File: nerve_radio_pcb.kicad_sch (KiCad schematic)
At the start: 25 parts, among them J1 BF030-20A-B1-0360-0277-0600-LB, J2 5V GPIO Breakout, J3 3V SPI Breakout, J4 Battery, U1 TXB0104QPWRQ1, U2 TPSM82903, U3 XBP9B-DMWT-002

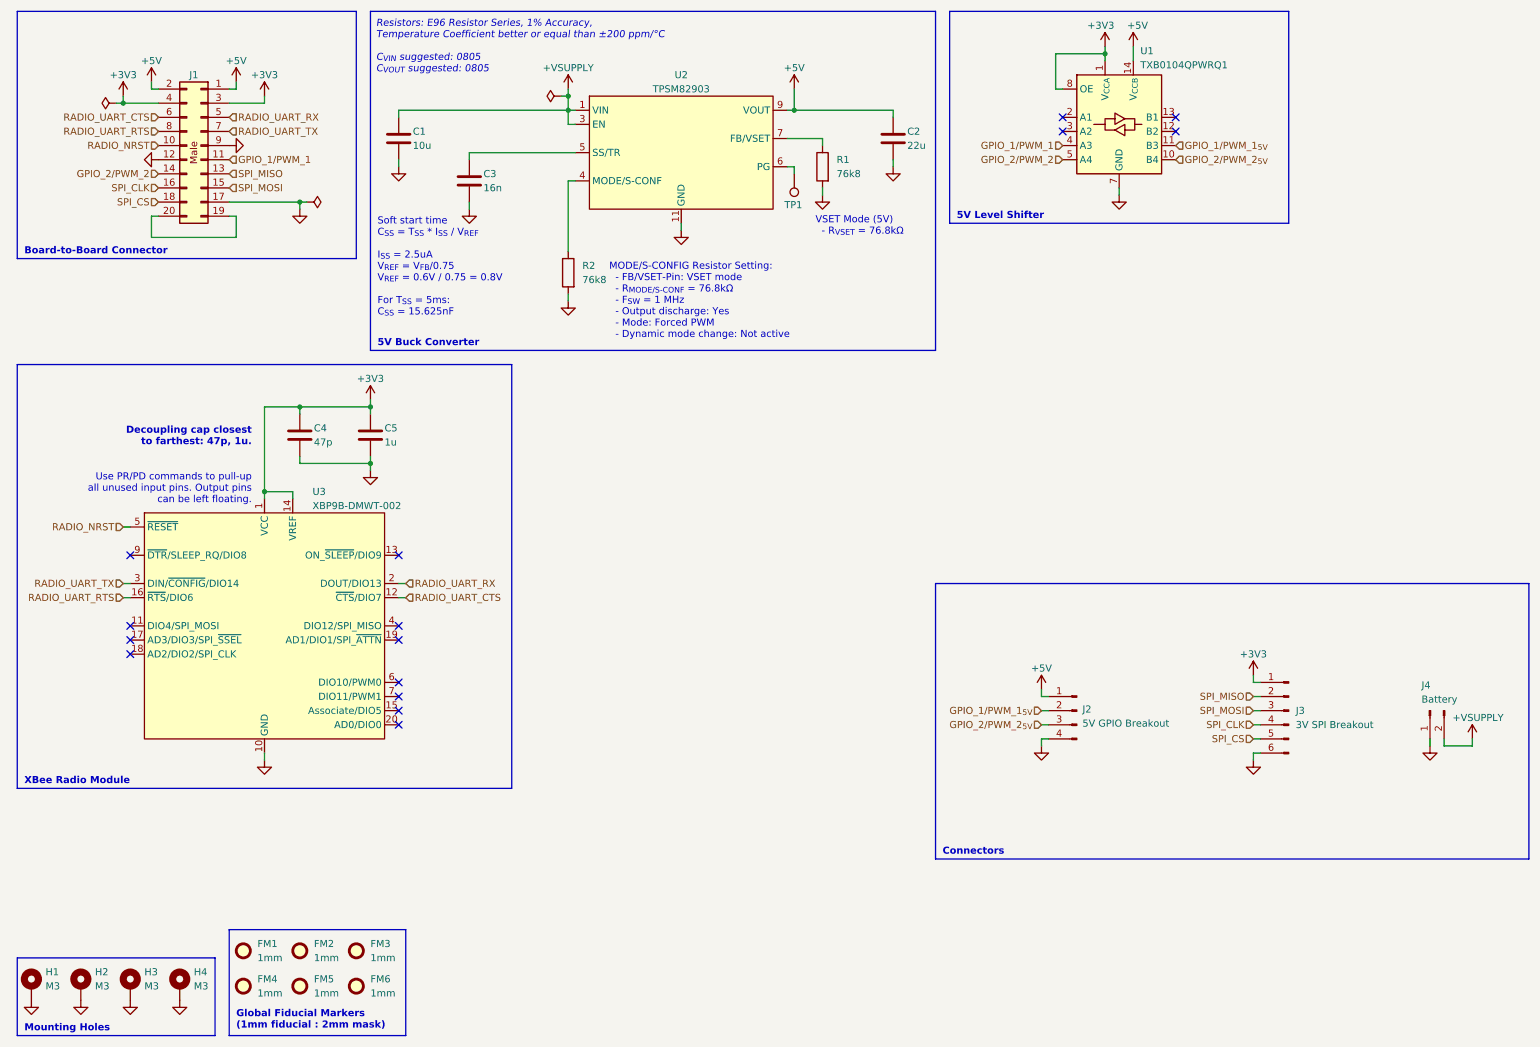
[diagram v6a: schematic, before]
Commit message: Update component recommendation notes
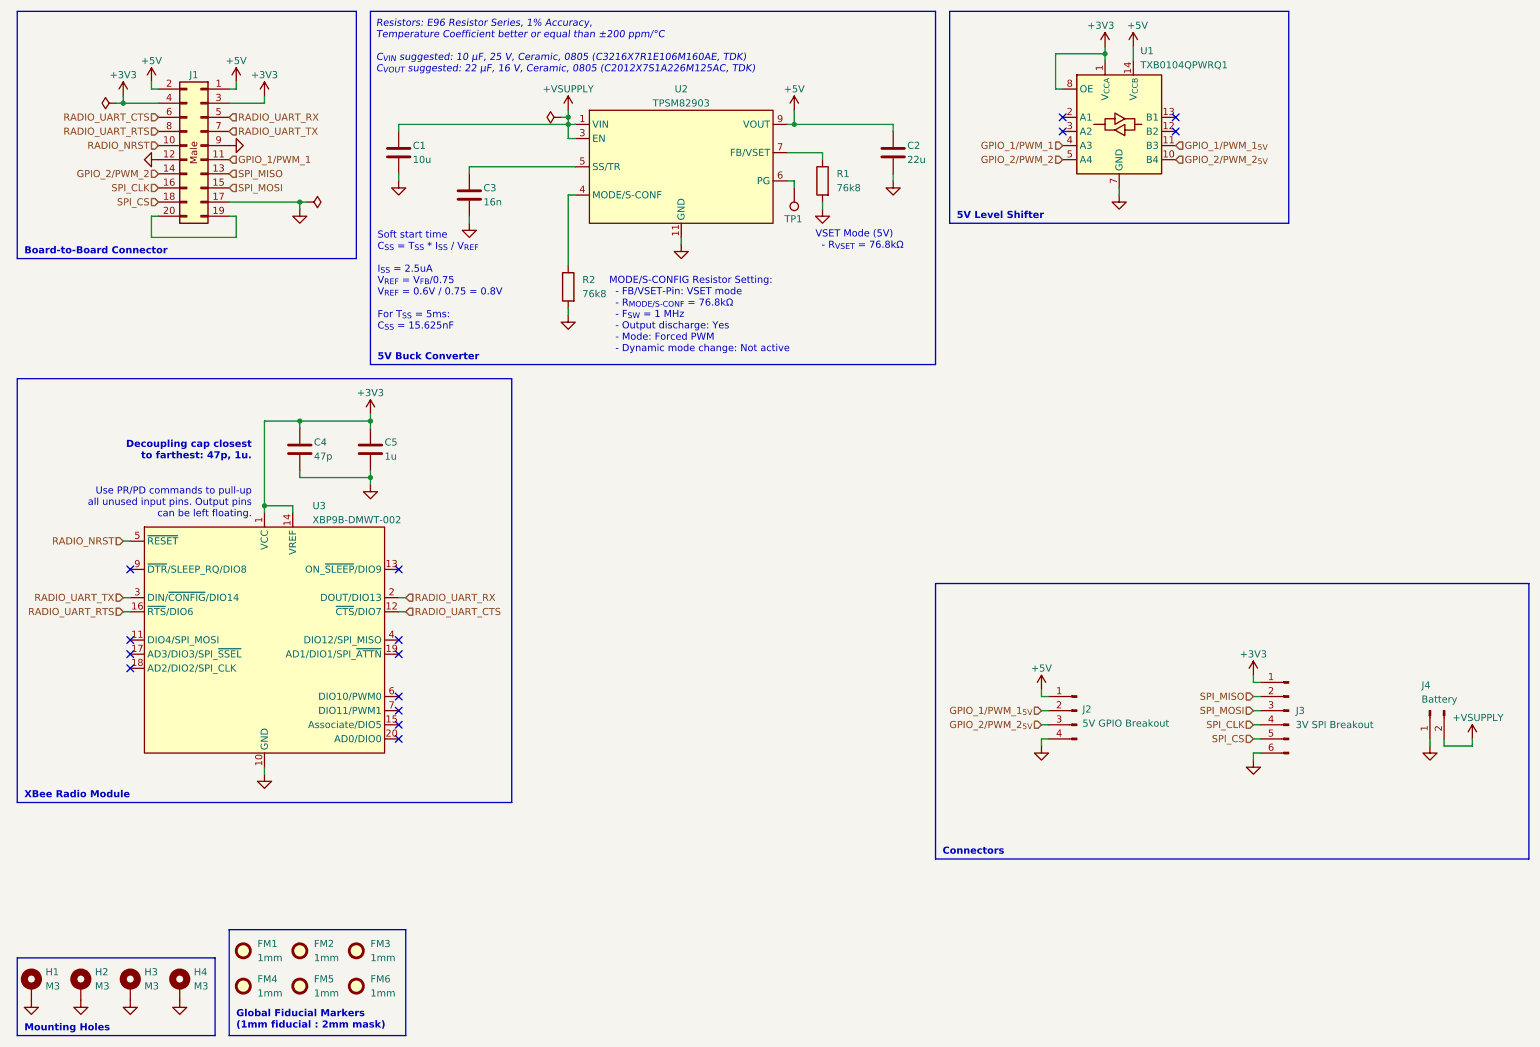
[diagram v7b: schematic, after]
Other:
- note added: "Resistors: E96 Resistor Series, 1% Accuracy, Temperature Coefficient better or equal than ±200 ppm/°C C_{VIN} suggested: 10 μF, 25 V, Ceramic, 0805 (C3216X7R1E106M160AE, TDK) C_{VOUT} suggested: 22 μF, 16 V, Ceramic, 0805 (C2012X7S1A226M125AC, TDK)"
- note removed: "Resistors: E96 Resistor Series, 1% Accuracy, Temperature Coefficient better or equal than ±200 ppm/°C C_{VIN} suggested: 0805 C_{VOUT} suggested: 0805"
- moved on the sheet: C1, C2, C3, C4, C5, R1, R2, TP1, U2, U3

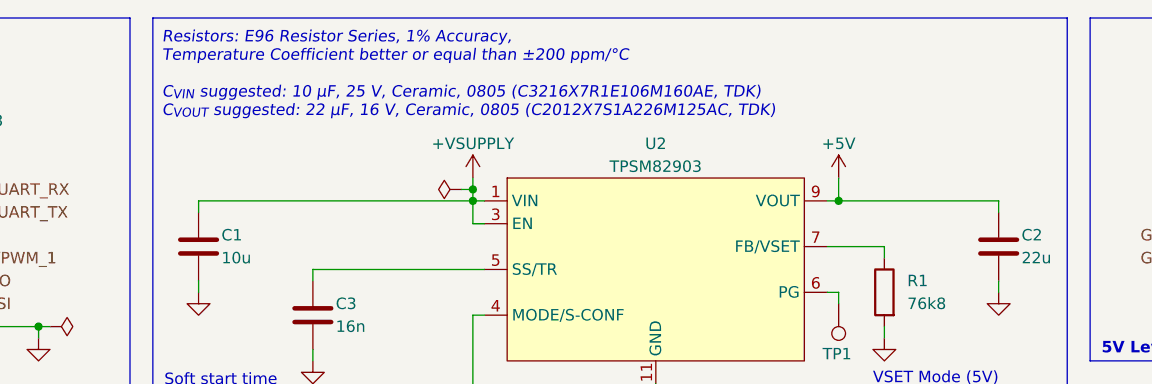
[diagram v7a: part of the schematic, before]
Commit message: Remove bad specific part suggestion notes
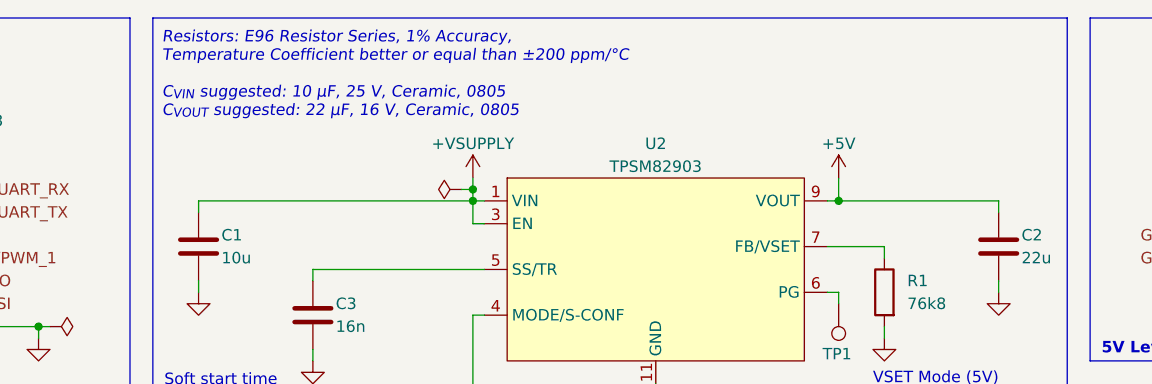
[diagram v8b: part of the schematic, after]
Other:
- note added: "Resistors: E96 Resistor Series, 1% Accuracy, Temperature Coefficient better or equal than ±200 ppm/°C C_{VIN} suggested: 10 μF, 25 V, Ceramic, 0805 C_{VOUT} suggested: 22 μF, 16 V, Ceramic, 0805"
- note removed: "Resistors: E96 Resistor Series, 1% Accuracy, Temperature Coefficient better or equal than ±200 ppm/°C C_{VIN} suggested: 10 μF, 25 V, Ceramic, 0805 (C3216X7R1E106M160AE, TDK) C_{VOUT} suggested: 22 μF, 16 V, Ceramic, 0805 (C2012X7S1A226M125AC, TDK)"
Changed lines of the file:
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@@
 		)
 	)
-	(text "Resistors: E96 Resistor Series, 1% Accuracy, \nTemperature Coefficient better or equal than ±200 ppm/°C\n\nC_{VIN} suggested: 10 μF, 25 V, Ceramic, 0805 (C3216X7R1E106M160AE, TDK)\nC_{VOUT} suggested: 22 μF, 16 V, Ceramic, 0805 (C2012X7S1A226M125AC, TDK)"
+	(text "Resistors: E96 Resistor Series, 1% Accuracy, \nTemperature Coefficient better or equal than ±200 ppm/°C\n\nC_{VIN} suggested: 10 μF, 25 V, Ceramic, 0805\nC_{VOUT} suggested: 22 μF, 16 V, Ceramic, 0805"
 		(exclude_from_sim no)
 		(at 77.216 19.05 0)
